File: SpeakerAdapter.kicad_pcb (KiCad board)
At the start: 2 copper layers, 2 parts, among them J1 Terminal Block, J2 JST-PH

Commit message: Position footprints.
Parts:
- moved J1 6.35 mm to (154.8, 60.0)
- moved J2 5.57 mm to (157.0, 67.0)
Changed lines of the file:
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@@
     (47 F.CrtYd user)
     (48 B.Fab user)
-    (49 F.Fab user)
+    (49 F.Fab user hide)
   )
   (setup
@@
   )
   (module TerminalBlock_4Ucon:TerminalBlock_4Ucon_1x04_P3.50mm_Horizontal (layer F.Cu)
-    (at 156.295001 66.155001)
+    (at 154.75 60)
     (descr "Terminal Block 4Ucon ItemNo. 20001, 4 pins, pitch 3.5mm, size 14.7x7mm^2, drill diamater 1.2mm, pad diameter 2.4mm, see http://www.4uconnector.com/online/object/4udrawing/20001.pdf, script-generated using https://github.com/pointhi/kicad-footprint-generator/scripts/TerminalBlock_4Ucon")
     (tags "THT Terminal Block 4Ucon ItemNo. 20001 pitch 3.5mm size 14.7x7mm^2 drill 1.2mm pad 2.4mm")
-    (fp_text reference J1 (at 5.25 -4.46) (layer F.SilkS)
+    (fp_text reference J1 (at 5.25 -4.46) (layer F.SilkS) hide
       (effects (font (size 1 1) (thickness 0.15)))
     )
@@
   )
   (module Connector_JST:JST_PH_B4B-PH-K_1x04_P2.00mm_Vertical (layer F.Cu)
-    (at 156.145001 72.505001)
+    (at 157 67)
     (descr "JST PH series connector, B4B-PH-K (http://www.jst-mfg.com/product/pdf/eng/ePH.pdf), generated with kicad-footprint-generator")
     (tags "connector JST PH side entry")
-    (fp_text reference J2 (at 3 -2.9) (layer F.SilkS)
+    (fp_text reference J2 (at 3 -2.9) (layer F.SilkS) hide
       (effects (font (size 1 1) (thickness 0.15)))
     )

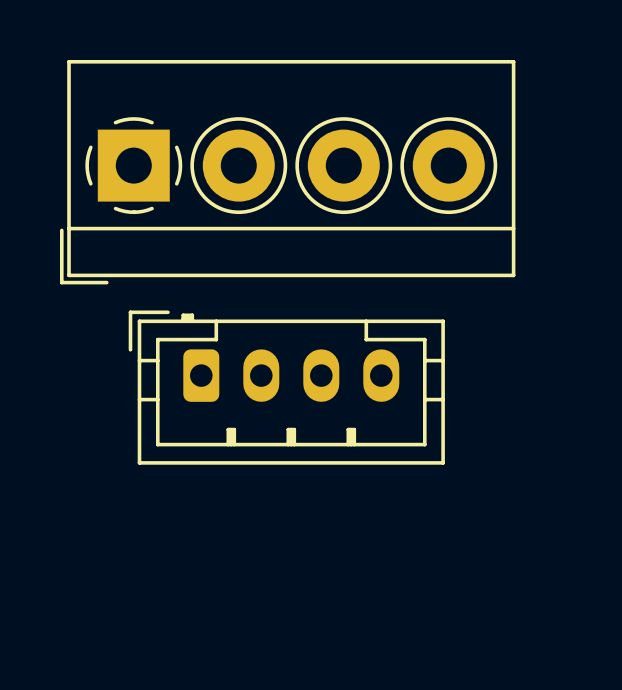
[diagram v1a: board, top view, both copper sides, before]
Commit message: Draw board edge.
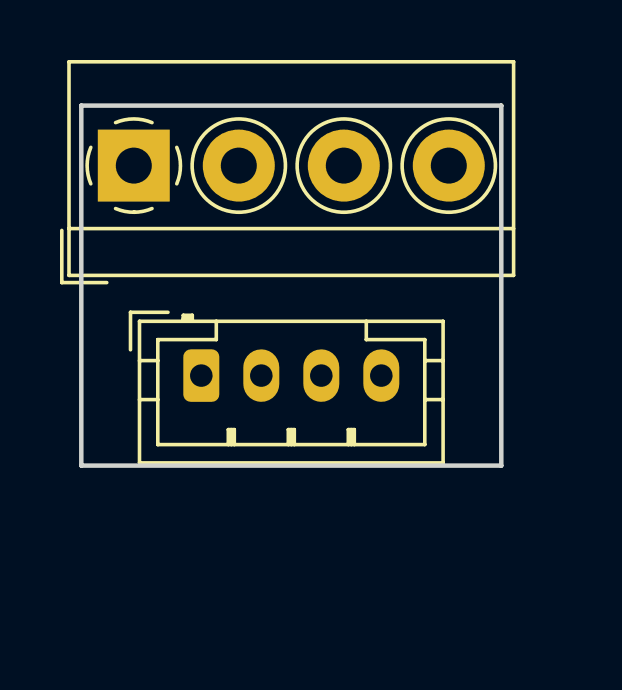
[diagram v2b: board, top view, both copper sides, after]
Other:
- board outline added: 14 x 12 mm
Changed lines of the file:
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@@
   (general
     (thickness 1.6)
-    (drawings 0)
+    (drawings 4)
     (tracks 0)
     (zones 0)
@@
     )
   )
+  (gr_line (start 153 70) (end 153 58) (layer Edge.Cuts) (width 0.15))
+  (gr_line (start 167 70) (end 153 70) (layer Edge.Cuts) (width 0.15))
+  (gr_line (start 167 58) (end 167 70) (layer Edge.Cuts) (width 0.15))
+  (gr_line (start 153 58) (end 167 58) (layer Edge.Cuts) (width 0.15))
 )

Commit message: Route tracks.
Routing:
- net Net-(J1-Pad4): track 0.00 -> 8.58 mm
- net Net-(J1-Pad1): track 0.00 -> 7.93 mm
- net Net-(J1-Pad3): track 0.00 -> 7.31 mm
- net Net-(J1-Pad2): track 0.00 -> 7.31 mm
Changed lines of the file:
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@@
     (thickness 1.6)
     (drawings 4)
-    (tracks 0)
+    (tracks 9)
     (zones 0)
     (modules 2)
@@
   )
   (setup
-    (last_trace_width 0.25)
+    (last_trace_width 0.5)
+    (user_trace_width 0.5)
     (trace_clearance 0.2)
     (zone_clearance 0.508)
@@
   (gr_line (start 167 58) (end 167 70) (layer Edge.Cuts) (width 0.15))
   (gr_line (start 153 58) (end 167 58) (layer Edge.Cuts) (width 0.15))
+  (segment (start 154.75 64.75) (end 157 67) (width 0.5) (layer B.Cu) (net 1))
+  (segment (start 154.75 60) (end 154.75 64.75) (width 0.5) (layer B.Cu) (net 1))
+  (segment (start 158.25 66.25) (end 159 67) (width 0.5) (layer B.Cu) (net 2))
+  (segment (start 158.25 60) (end 158.25 66.25) (width 0.5) (layer B.Cu) (net 2))
+  (segment (start 161.75 66.25) (end 161 67) (width 0.5) (layer B.Cu) (net 3))
+  (segment (start 161.75 60) (end 161.75 66.25) (width 0.5) (layer B.Cu) (net 3))
+  (segment (start 164.1 67) (end 163 67) (width 0.5) (layer B.Cu) (net 4))
+  (segment (start 165.25 65.85) (end 164.1 67) (width 0.5) (layer B.Cu) (net 4))
+  (segment (start 165.25 60) (end 165.25 65.85) (width 0.5) (layer B.Cu) (net 4))
 )

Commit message: Add metadata on back silkscreen.
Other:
- board text added: "Speaker Adapter PEP 2019-08-24"
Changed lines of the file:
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@@
   (general
     (thickness 1.6)
-    (drawings 4)
+    (drawings 5)
     (tracks 9)
     (zones 0)
@@
     )
   )
+  (gr_text "Speaker Adapter\nPEP 2019-08-24" (at 160 64) (layer B.SilkS)
+    (effects (font (size 1 1) (thickness 0.2)) (justify mirror))
+  )
   (gr_line (start 153 70) (end 153 58) (layer Edge.Cuts) (width 0.15))
